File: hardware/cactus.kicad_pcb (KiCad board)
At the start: 2 copper layers, 76.5 x 38.1 mm, 21 parts, among them SW1 SW_Push, U1 WeMos_Battery_Shield, U2 WeMos_D1_mini, U3 74HC595, U4 Si7021_breakout

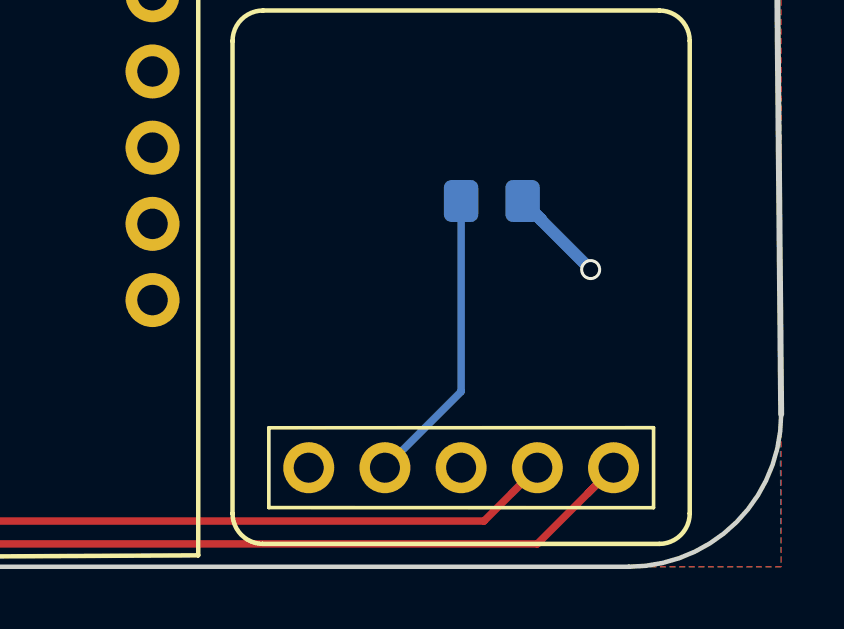
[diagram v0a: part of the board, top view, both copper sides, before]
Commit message: Note on back silkscreen on enabling 4-pin Si7021 boards
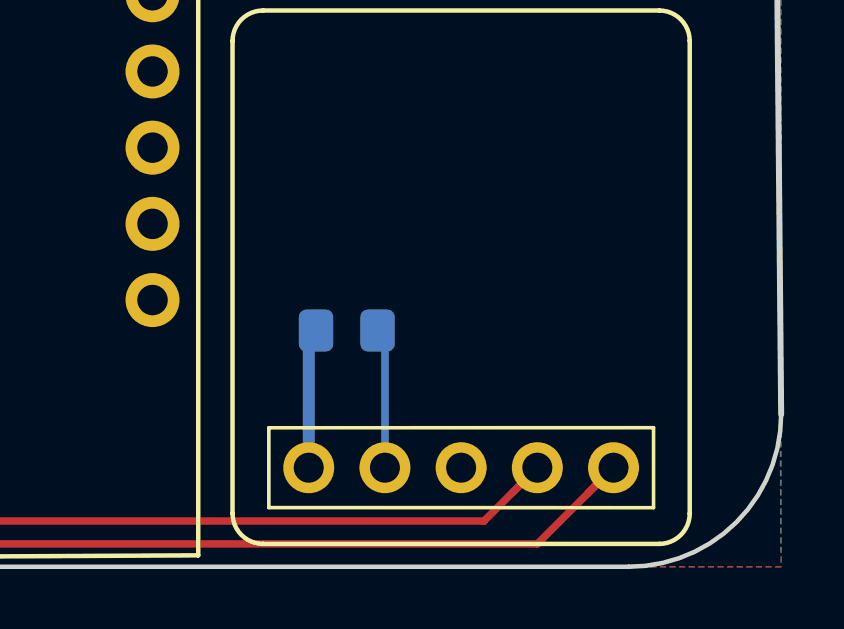
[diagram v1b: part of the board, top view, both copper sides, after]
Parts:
- moved R9 6.48 mm to (176.0, 81.0), turned to 0 degrees
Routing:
- net Net-(R9-Pad2): track 9.94 -> 4.67 mm
- net VCC: track 18.3 -> 18.8 mm, vias 2 -> 1
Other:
- board text added: "Enable 4-pin Si7021 board"
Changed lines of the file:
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@@
   (general
     (thickness 1.6)
-    (drawings 18)
-    (tracks 182)
+    (drawings 19)
+    (tracks 179)
     (zones 0)
     (modules 21)
@@
     (33 F.Adhes user hide)
     (34 B.Paste user)
-    (35 F.Paste user hide)
+    (35 F.Paste user)
     (36 B.SilkS user)
-    (37 F.SilkS user hide)
+    (37 F.SilkS user)
     (38 B.Mask user)
     (39 F.Mask user hide)
@@
   )
   (module Resistor_SMD:R_0805_2012Metric_Pad1.15x1.40mm_HandSolder (layer B.Cu)
-    (at 180.857 76.708 180)
+    (at 176.022 81.026)
     (descr "Resistor SMD 0805 (2012 Metric), square (rectangular) end terminal, IPC_7351 nominal with elongated pad for handsoldering. (Body size source: https://docs.google.com/spreadsheets/d/1BsfQQcO9C6DZCsRaXUlFlo91Tg2WpOkGARC1WS5S8t0/edit?usp=sharing), generated with kicad-footprint-generator")
     (tags "resistor handsolder")
     (attr smd)
-    (fp_text reference R9 (at 0 1.65 180) (layer B.SilkS)
-      (effects (font (size 1 1) (thickness 0.15)) (justify mirror))
-    )
-    (fp_text value 0ohm (at 0 -1.65 180) (layer B.Fab)
+    (fp_text reference R9 (at 0 -1.778) (layer B.SilkS)
+      (effects (font (size 1 1) (thickness 0.15)) (justify mirror))
+    )
+    (fp_text value 0ohm (at 0 -1.65) (layer B.Fab)
       (effects (font (size 1 1) (thickness 0.15)) (justify mirror))
     )
@@
     (fp_line (start 1.85 0.95) (end 1.85 -0.95) (layer B.CrtYd) (width 0.05))
     (fp_line (start 1.85 -0.95) (end -1.85 -0.95) (layer B.CrtYd) (width 0.05))
-    (fp_text user %R (at 0 0 180) (layer B.Fab)
+    (fp_text user %R (at 0 0) (layer B.Fab)
       (effects (font (size 0.5 0.5) (thickness 0.08)) (justify mirror))
     )
-    (pad 1 smd roundrect (at -1.025 0 180) (size 1.15 1.4) (layers B.Cu B.Paste B.Mask) (roundrect_rratio 0.217391)
+    (pad 1 smd roundrect (at -1.025 0) (size 1.15 1.4) (layers B.Cu B.Paste B.Mask) (roundrect_rratio 0.217391)
       (net 17 VCC))
-    (pad 2 smd roundrect (at 1.025 0 180) (size 1.15 1.4) (layers B.Cu B.Paste B.Mask) (roundrect_rratio 0.217391)
+    (pad 2 smd roundrect (at 1.025 0) (size 1.15 1.4) (layers B.Cu B.Paste B.Mask) (roundrect_rratio 0.217391)
       (net 18 "Net-(R9-Pad2)"))
     (model ${KISYS3DMOD}/Resistor_SMD.3dshapes/R_0805_2012Metric.wrl
@@
       (xy -2.549664 -1.91989) (xy -2.469928 -1.911165) (xy -2.400256 -1.919918)) (layer B.SilkS) (width 0.01))
   )
+  (gr_text "Enable 4-pin\nSi7021 board" (at 184.404 81.026) (layer B.SilkS)
+    (effects (font (size 0.6 0.6) (thickness 0.1)) (justify left mirror))
+  )
   (gr_text "Cactus@Hutscape V1.0 2019" (at 188.214 59.436) (layer B.SilkS)
     (effects (font (size 0.7 0.7) (thickness 0.1)) (justify left mirror))
@@
     (effects (font (size 0.7 0.7) (thickness 0.1)) (justify left mirror))
   )
-  (gr_text "Si7021 board" (at 179.832 82.804) (layer B.SilkS)
+  (gr_text "Si7021 board" (at 179.578 72.39) (layer B.SilkS)
     (effects (font (size 1 1) (thickness 0.15)) (justify mirror))
   )
@@
   (segment (start 118.491 79.9465) (end 124.0155 79.9465) (width 0.4) (layer F.Cu) (net 16))
   (segment (start 125.984 77.978) (end 129.032 77.978) (width 0.4) (layer B.Cu) (net 16))
-  (segment (start 182.505372 77.331372) (end 182.505372 77.349372) (width 0.4) (layer B.Cu) (net 17))
-  (segment (start 181.882 76.708) (end 182.505372 77.331372) (width 0.4) (layer B.Cu) (net 17))
-  (segment (start 181.882 76.726) (end 184.15 78.994) (width 0.4) (layer B.Cu) (net 17))
-  (via (at 184.15 78.994) (size 0.7) (drill 0.5) (layers F.Cu B.Cu) (net 17))
-  (segment (start 181.882 76.708) (end 181.882 76.726) (width 0.4) (layer B.Cu) (net 17))
   (segment (start 161.417 69.756) (end 161.417 71.501) (width 0.4) (layer B.Cu) (net 17))
   (segment (start 161.417 71.501) (end 160.274 72.644) (width 0.4) (layer B.Cu) (net 17))
@@
   (segment (start 161.417 68.199) (end 161.417 69.756) (width 0.4) (layer B.Cu) (net 17))
   (segment (start 161.036 67.818) (end 161.417 68.199) (width 0.4) (layer B.Cu) (net 17))
-  (segment (start 179.832 83.058) (end 177.292 85.598) (width 0.25) (layer B.Cu) (net 18))
-  (segment (start 179.832 76.708) (end 179.832 83.058) (width 0.25) (layer B.Cu) (net 18))
+  (segment (start 174.752 81.271) (end 174.997 81.026) (width 0.4) (layer B.Cu) (net 17))
+  (segment (start 174.752 85.598) (end 174.752 81.271) (width 0.4) (layer B.Cu) (net 17))
+  (segment (start 177.292 81.271) (end 177.047 81.026) (width 0.25) (layer B.Cu) (net 18))
+  (segment (start 177.292 85.598) (end 177.292 81.271) (width 0.25) (layer B.Cu) (net 18))
   (segment (start 117.591001 63.806501) (end 115.876501 63.806501) (width 0.25) (layer F.Cu) (net 19))
   (segment (start 118.491 64.7065) (end 117.591001 63.806501) (width 0.25) (layer F.Cu) (net 19))

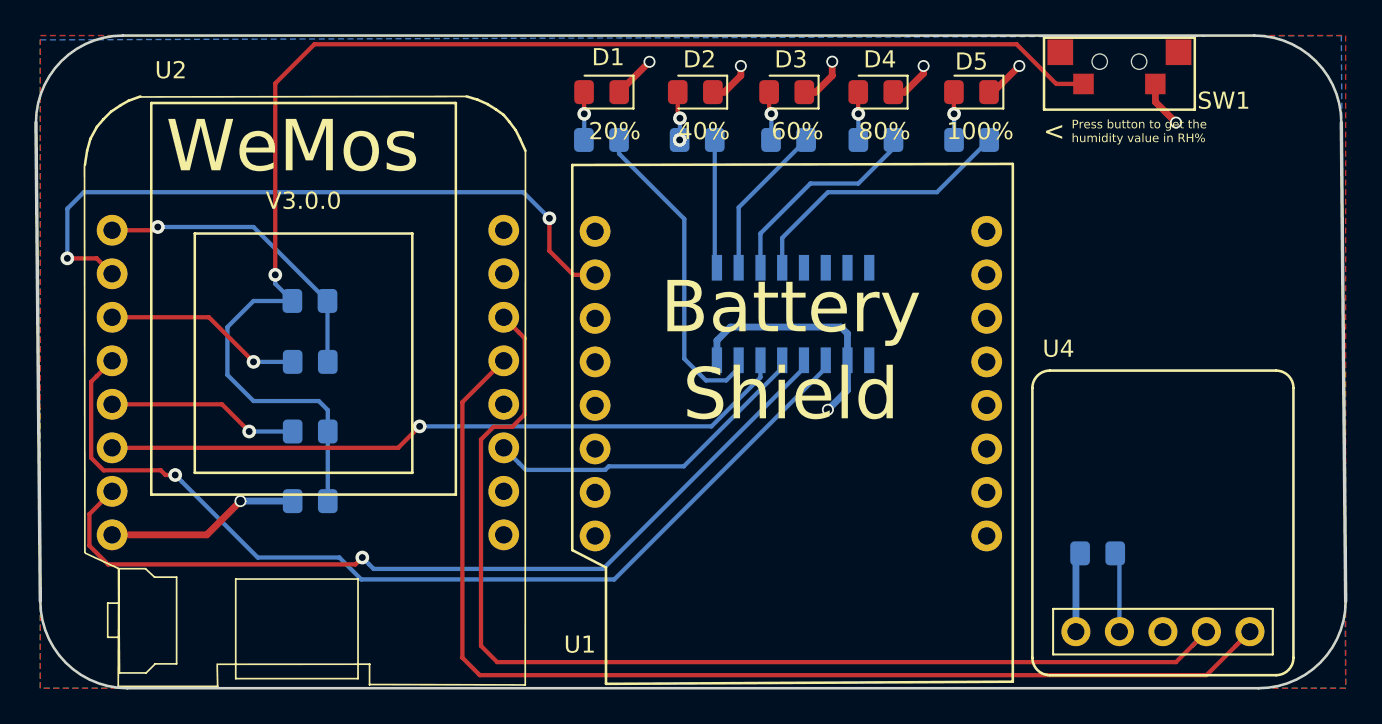
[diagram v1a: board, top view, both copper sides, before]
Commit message: Add mounting holes, more silkscreen annotations
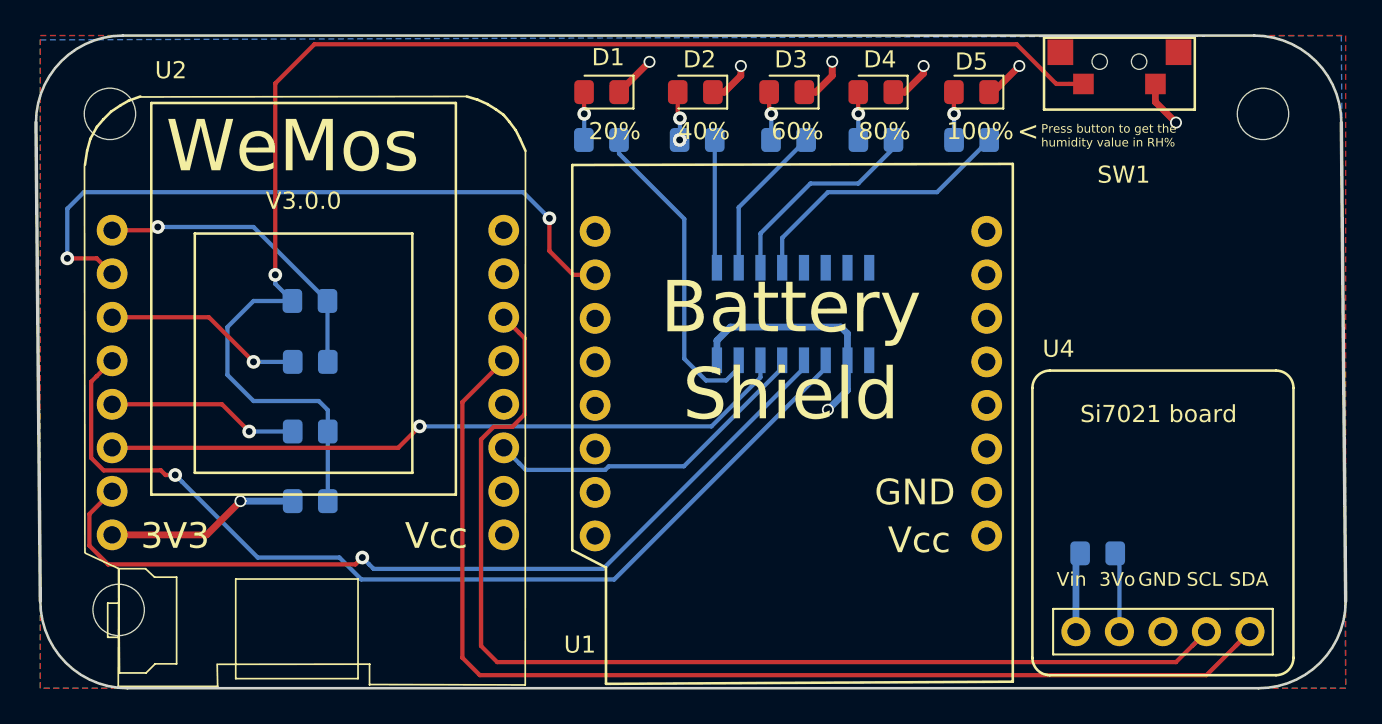
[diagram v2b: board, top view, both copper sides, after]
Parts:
- added REF**: MountingHole_3mm, MountingHole:MountingHole_3mm, F.Cu at (118.9, 84.3)
- added REF**: MountingHole_3mm, MountingHole:MountingHole_3mm, F.Cu at (118.4, 55.4)
- added REF**: MountingHole_3mm, MountingHole:MountingHole_3mm, F.Cu at (185.7, 55.4)
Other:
- board text added: "3V3"
- board text added: "GND"
- board text added: "QA"
- board text added: "QB"
- board text added: "QC"
- board text added: "QD"
- board text added: "QE"
- board text added: "Vcc"

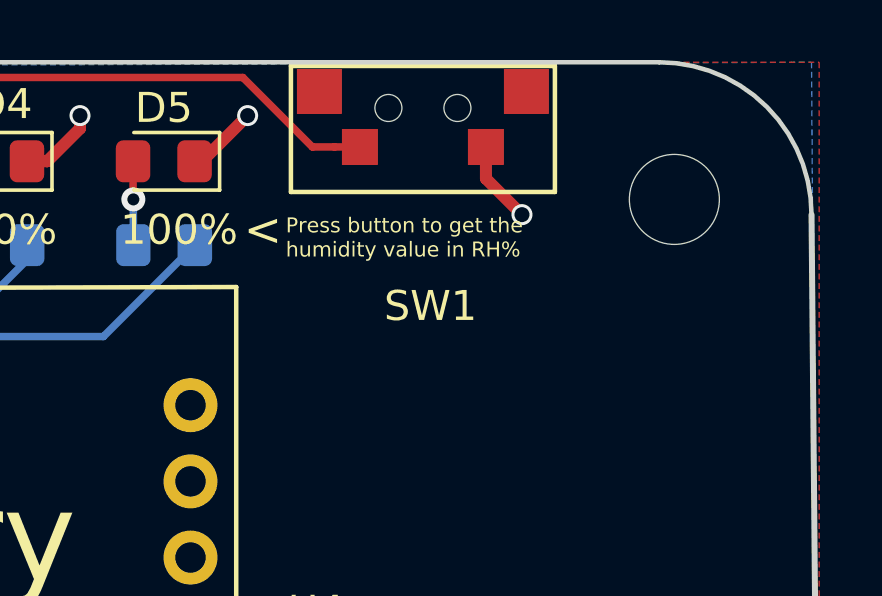
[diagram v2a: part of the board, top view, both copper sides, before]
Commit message: [mech] Add note on long press button on silkscreen
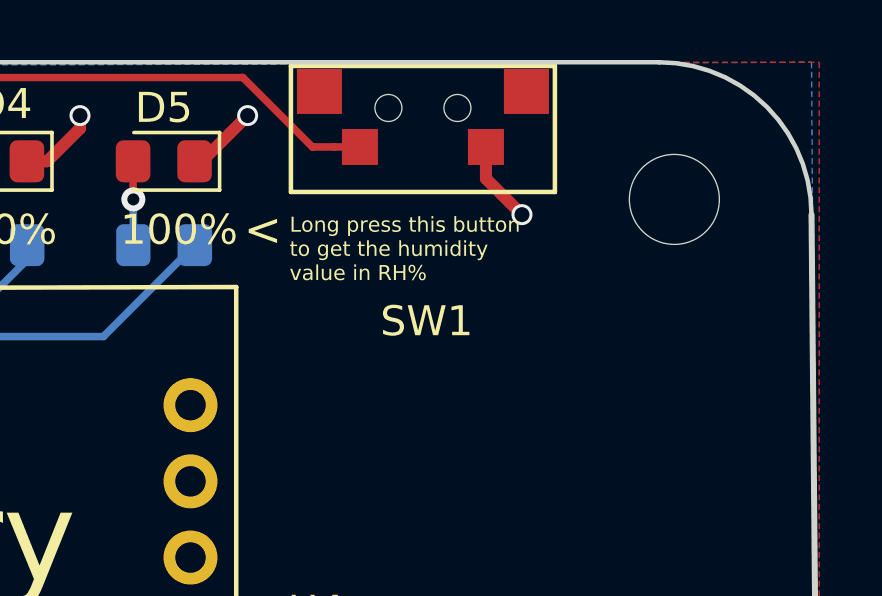
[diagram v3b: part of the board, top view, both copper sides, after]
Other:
- board text added: "Long press this button to get the humidity value in RH%"
- board text removed: "Press button to get the humidity value in RH%"
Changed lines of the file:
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@@
   (page A4)
   (layers
-    (0 F.Cu signal)
+    (0 F.Cu signal hide)
     (31 B.Cu signal hide)
     (32 B.Adhes user hide)
@@
   (module Switch_Tactile_pushbutton:Tactile_pushbutton (layer F.Cu)
     (at 177.292 52.324)
-    (fp_text reference SW1 (at 0.254 6.604) (layer F.SilkS)
+    (fp_text reference SW1 (at 0.127 7.112) (layer F.SilkS)
       (effects (font (size 1 1) (thickness 0.15)))
     )
@@
     (effects (font (size 1.1 1.1) (thickness 0.2)))
   )
-  (gr_text "Press button to get the\nhumidity value in RH%" (at 172.72 56.642) (layer F.SilkS)
+  (gr_text "Long press this button \nto get the humidity \nvalue in RH%" (at 172.847 57.023) (layer F.SilkS)
     (effects (font (size 0.5 0.5) (thickness 0.08)) (justify left))
   )

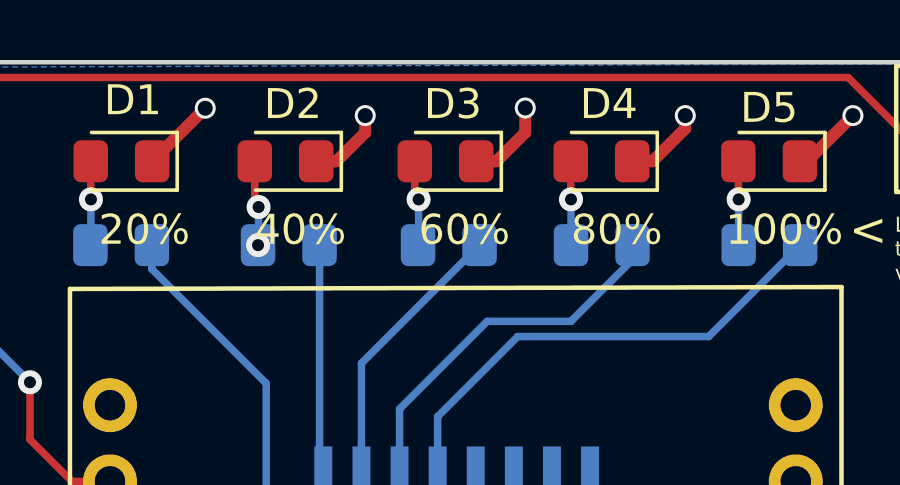
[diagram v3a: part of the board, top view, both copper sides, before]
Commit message: [mech] Distribute LEDs and their resistors horizontally
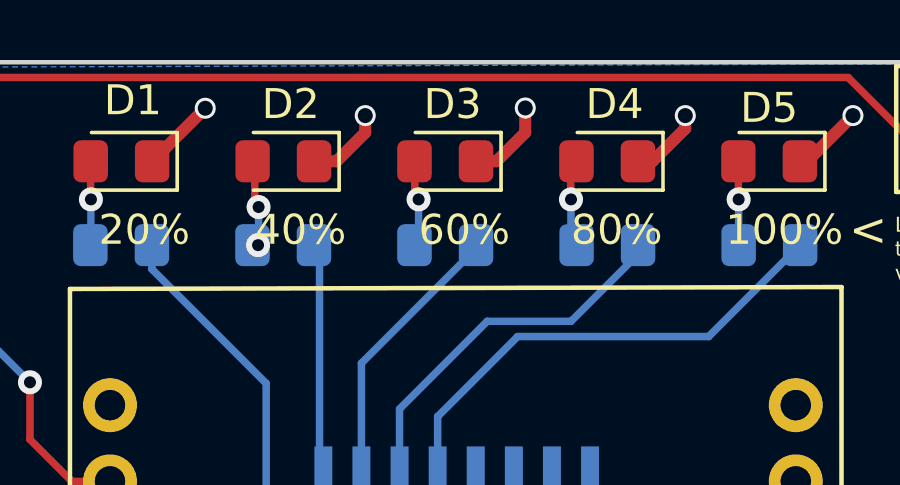
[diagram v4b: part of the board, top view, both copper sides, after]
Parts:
- moved D4 0.19 mm to (163.3, 54.1)
- moved R2 0.19 mm to (152.5, 56.9)
- moved R4 0.19 mm to (163.3, 56.9)
- moved R3 0.12 mm to (157.9, 56.9)
- moved D2 0.07 mm to (152.5, 54.1)
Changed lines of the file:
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@@
   (layers
     (0 F.Cu signal hide)
-    (31 B.Cu signal hide)
-    (32 B.Adhes user hide)
-    (33 F.Adhes user)
-    (34 B.Paste user hide)
-    (35 F.Paste user)
-    (36 B.SilkS user hide)
-    (37 F.SilkS user)
+    (31 B.Cu signal)
+    (32 B.Adhes user)
+    (33 F.Adhes user hide)
+    (34 B.Paste user)
+    (35 F.Paste user hide)
+    (36 B.SilkS user)
+    (37 F.SilkS user hide)
     (38 B.Mask user)
-    (39 F.Mask user)
+    (39 F.Mask user hide)
     (40 Dwgs.User user)
     (41 Cmts.User user)
@@
     (45 Margin user)
     (46 B.CrtYd user hide)
-    (47 F.CrtYd user)
+    (47 F.CrtYd user hide)
     (48 B.Fab user hide)
     (49 F.Fab user hide)
@@
   )
   (module LED_SMD:LED_0805_2012Metric_Pad1.15x1.40mm_HandSolder (layer F.Cu)
-    (at 152.536 54.102 180)
+    (at 152.4635 54.102 180)
     (descr "LED SMD 0805 (2012 Metric), square (rectangular) end terminal, IPC_7351 nominal, (Body size source: https://docs.google.com/spreadsheets/d/1BsfQQcO9C6DZCsRaXUlFlo91Tg2WpOkGARC1WS5S8t0/edit?usp=sharing), generated with kicad-footprint-generator")
     (tags "LED handsolder")
@@
   )
   (module LED_SMD:LED_0805_2012Metric_Pad1.15x1.40mm_HandSolder (layer F.Cu)
-    (at 157.87 54.102 180)
+    (at 157.861 54.102 180)
     (descr "LED SMD 0805 (2012 Metric), square (rectangular) end terminal, IPC_7351 nominal, (Body size source: https://docs.google.com/spreadsheets/d/1BsfQQcO9C6DZCsRaXUlFlo91Tg2WpOkGARC1WS5S8t0/edit?usp=sharing), generated with kicad-footprint-generator")
     (tags "LED handsolder")
@@
   )
   (module LED_SMD:LED_0805_2012Metric_Pad1.15x1.40mm_HandSolder (layer F.Cu)
-    (at 163.068 54.102 180)
+    (at 163.2585 54.102 180)
     (descr "LED SMD 0805 (2012 Metric), square (rectangular) end terminal, IPC_7351 nominal, (Body size source: https://docs.google.com/spreadsheets/d/1BsfQQcO9C6DZCsRaXUlFlo91Tg2WpOkGARC1WS5S8t0/edit?usp=sharing), generated with kicad-footprint-generator")
     (tags "LED handsolder")
@@
   )
   (module Resistor_SMD:R_0805_2012Metric_Pad1.15x1.40mm_HandSolder (layer B.Cu)
-    (at 152.645 56.896 180)
+    (at 152.459 56.896 180)
     (descr "Resistor SMD 0805 (2012 Metric), square (rectangular) end terminal, IPC_7351 nominal with elongated pad for handsoldering. (Body size source: https://docs.google.com/spreadsheets/d/1BsfQQcO9C6DZCsRaXUlFlo91Tg2WpOkGARC1WS5S8t0/edit?usp=sharing), generated with kicad-footprint-generator")
     (tags "resistor handsolder")
@@
   )
   (module Resistor_SMD:R_0805_2012Metric_Pad1.15x1.40mm_HandSolder (layer B.Cu)
-    (at 157.979 56.896 180)
+    (at 157.861 56.896 180)
     (descr "Resistor SMD 0805 (2012 Metric), square (rectangular) end terminal, IPC_7351 nominal with elongated pad for handsoldering. (Body size source: https://docs.google.com/spreadsheets/d/1BsfQQcO9C6DZCsRaXUlFlo91Tg2WpOkGARC1WS5S8t0/edit?usp=sharing), generated with kicad-footprint-generator")
     (tags "resistor handsolder")
@@
   )
   (module Resistor_SMD:R_0805_2012Metric_Pad1.15x1.40mm_HandSolder (layer B.Cu)
-    (at 163.077 56.896 180)
+    (at 163.263 56.896 180)
     (descr "Resistor SMD 0805 (2012 Metric), square (rectangular) end terminal, IPC_7351 nominal with elongated pad for handsoldering. (Body size source: https://docs.google.com/spreadsheets/d/1BsfQQcO9C6DZCsRaXUlFlo91Tg2WpOkGARC1WS5S8t0/edit?usp=sharing), generated with kicad-footprint-generator")
     (tags "resistor handsolder")
@@
   (segment (start 135.1915 74.8665) (end 118.491 74.8665) (width 0.25) (layer F.Cu) (net 21))
   (segment (start 136.442999 73.615001) (end 135.1915 74.8665) (width 0.25) (layer F.Cu) (net 21))
+  (segment (start 153.477999 73.615001) (end 136.442999 73.615001) (width 0.25) (layer B.Cu) (net 21))
   (segment (start 156.337 70.756) (end 153.477999 73.615001) (width 0.25) (layer B.Cu) (net 21))
   (segment (start 156.337 69.756) (end 156.337 70.756) (width 0.25) (layer B.Cu) (net 21))
-  (segment (start 153.477999 73.615001) (end 136.442999 73.615001) (width 0.25) (layer B.Cu) (net 21))
   (via (at 133.096 81.271499) (size 0.8) (drill 0.4) (layers F.Cu B.Cu) (net 22))
   (segment (start 118.491 77.4065) (end 117.165999 78.731501) (width 0.25) (layer F.Cu) (net 22))

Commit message: [mech] Pass ERC with checks for courtyards
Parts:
- renumbered REF** to LOGO
